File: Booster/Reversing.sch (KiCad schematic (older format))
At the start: 20 parts, among them J701 Conn_01x04, P701 REVERSER_OUT, P702 REVERSER_OUT_OP, Q701 BC817-40, SW701 SW_SPST_x03, U203 LM339, U701 74HC86, U702 PC817

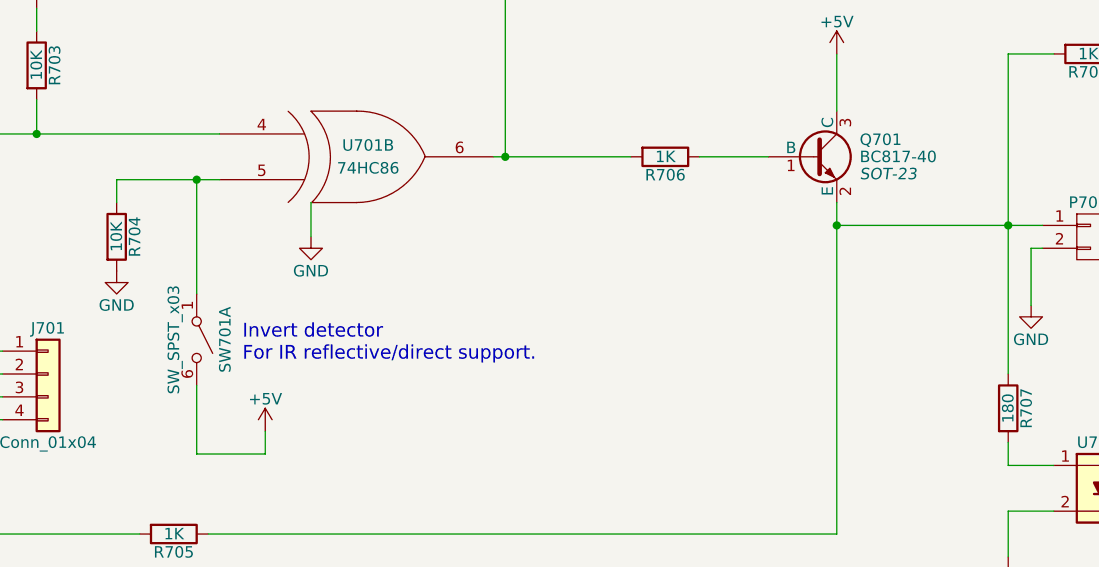
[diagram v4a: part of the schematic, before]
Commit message: Assigned footprints & minor adjustments.
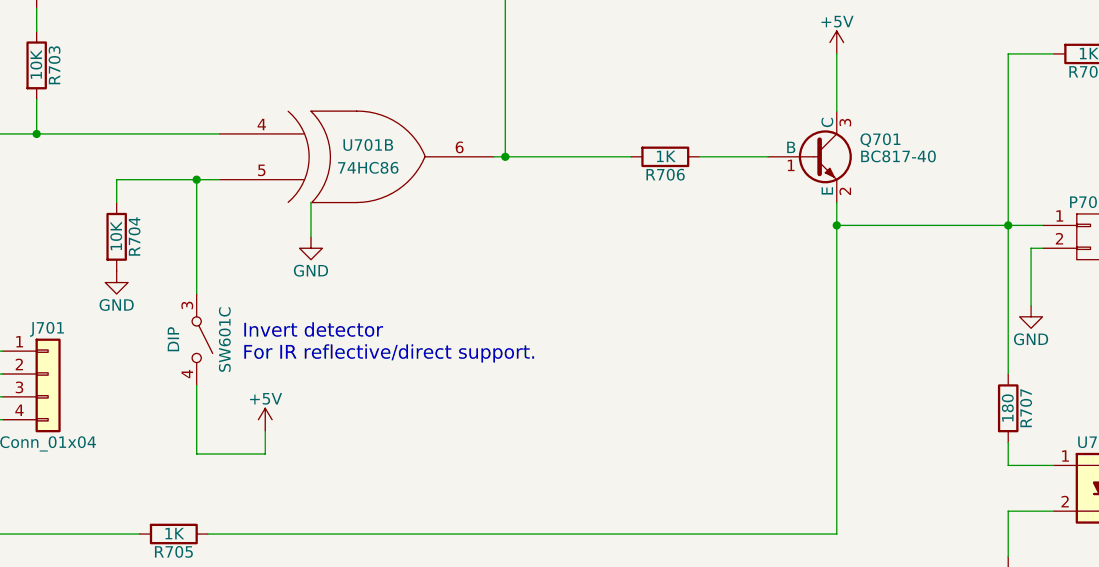
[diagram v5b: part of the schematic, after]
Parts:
- D701: footprint (none) -> LEDs:LED_D3.0mm
- J701: footprint (none) -> Connectors_JST:JST_XH_B04B-XH-A_04x2.50mm_Straight
- P701, P702: footprint (none) -> Connectors_JST:JST_XH_B02B-XH-A_02x2.50mm_Straight
- Q701: footprint SOT-23 -> TO_SOT_Packages_SMD:SOT-23
- R701, R702, R703, R704, R705, R706, R707, R708: footprint (none) -> Resistors_SMD:R_0805
- RV701: footprint (none) -> Potentiometers:Potentiometer_Trimmer_Bourns_3296W
- SW601: renamed from SW701; value SW_SPST_x03 -> DIP; footprint (none) -> Buttons_Switches_THT:SW_DIP_x3_W7.62mm_Slide
- TP701, TP702: footprint (none) -> Measurement_Points:Measurement_Point_Round-TH_Small
- U203, U701: footprint (none) -> SMD_Packages:SOIC-14_N
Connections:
- net +5V: now also SW601.4 (B); no longer SW601.6 (B)
- net at R704.1, U701.5 (IN2): now also SW601.3 (A); no longer SW601.1 (A)
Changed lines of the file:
@@
 F 0 "U701" H 8250 2300 50  0000 C CNN
 F 1 "74HC86" H 8250 2200 50  0000 C CNN
-F 2 "" H 8200 2250 50  0000 C CNN
+F 2 "SMD_Packages:SOIC-14_N" H 8200 2250 50  0001 C CNN
 F 3 "" H 8200 2250 50  0000 C CNN
 	4    8200 2250
@@
 F 0 "R701" V 2330 4300 50  0000 C CNN
 F 1 "10K" V 2250 4300 50  0000 C CNN
-F 2 "" V 2180 4300 50  0000 C CNN
+F 2 "Resistors_SMD:R_0805" V 2180 4300 50  0001 C CNN
 F 3 "" H 2250 4300 50  0000 C CNN
 	1    2250 4300
@@
 F 0 "U203" H 3500 3550 50  0000 L CNN
 F 1 "LM339" H 3500 3150 50  0000 L CNN
-F 2 "" H 3450 3450 50  0000 C CNN
+F 2 "SMD_Packages:SOIC-14_N" H 3450 3450 50  0001 C CNN
 F 3 "" H 3550 3550 50  0000 C CNN
 	1    3500 3350
@@
 F 0 "R703" V 4130 3050 50  0000 C CNN
 F 1 "10K" V 4050 3050 50  0000 C CNN
-F 2 "" V 3980 3050 50  0000 C CNN
+F 2 "Resistors_SMD:R_0805" V 3980 3050 50  0001 C CNN
 F 3 "" H 4050 3050 50  0000 C CNN
 	1    4050 3050
@@
 $EndComp
 $Comp
-L +5V #PWR054
+L +5V #PWR055
 U 1 1 5A08A3B3
 P 4050 2800
-F 0 "#PWR054" H 4050 2650 50  0001 C CNN
+F 0 "#PWR055" H 4050 2650 50  0001 C CNN
 F 1 "+5V" H 4050 2940 50  0000 C CNN
 F 2 "" H 4050 2800 50  0000 C CNN
@@
 F 0 "RV701" V 2375 3250 50  0000 C CNN
 F 1 "POT_TRIM" V 2450 3250 50  0000 C CNN
-F 2 "" H 2550 3250 50  0000 C CNN
+F 2 "Potentiometers:Potentiometer_Trimmer_Bourns_3296W" H 2550 3250 50  0001 C CNN
 F 3 "" H 2550 3250 50  0000 C CNN
 	1    2550 3250
@@
 F 0 "R706" V 6880 3450 50  0000 C CNN
 F 1 "1K" V 6800 3450 50  0000 C CNN
-F 2 "" V 6730 3450 50  0000 C CNN
+F 2 "Resistors_SMD:R_0805" V 6730 3450 50  0001 C CNN
 F 3 "" H 6800 3450 50  0000 C CNN
 	1    6800 3450
@@
 F 0 "D701" H 9100 3100 50  0000 C CNN
 F 1 "LED" H 9100 2900 50  0000 C CNN
-F 2 "" H 9100 3000 50  0000 C CNN
+F 2 "LEDs:LED_D3.0mm" H 9100 3000 50  0001 C CNN
 F 3 "" H 9100 3000 50  0000 C CNN
 	1    9100 3000
@@
 F 0 "R708" V 8730 3000 50  0000 C CNN
 F 1 "1K" V 8650 3000 50  0000 C CNN
-F 2 "" V 8580 3000 50  0000 C CNN
+F 2 "Resistors_SMD:R_0805" V 8580 3000 50  0001 C CNN
 F 3 "" H 8650 3000 50  0000 C CNN
 	1    8650 3000
@@
 $EndComp
 $Comp
-L +5V #PWR055
+L +5V #PWR056
 U 1 1 5A08AC26
 P 7550 3000
-F 0 "#PWR055" H 7550 2850 50  0001 C CNN
+F 0 "#PWR056" H 7550 2850 50  0001 C CNN
 F 1 "+5V" H 7550 3140 50  0000 C CNN
 F 2 "" H 7550 3000 50  0000 C CNN
@@
 $EndComp
 $Comp
-L GND #PWR056
+L GND #PWR057
 U 1 1 5A08AC50
 P 9350 3800
-F 0 "#PWR056" H 9350 3550 50  0001 C CNN
+F 0 "#PWR057" H 9350 3550 50  0001 C CNN
 F 1 "GND" H 9350 3650 50  0000 C CNN
 F 2 "" H 9350 3800 50  0000 C CNN
@@
 F 0 "P701" H 8650 3950 50  0000 C CNN
 F 1 "REVERSER_OUT" V 8750 3800 50  0000 C CNN
-F 2 "" H 8650 3800 50  0000 C CNN
+F 2 "Connectors_JST:JST_XH_B02B-XH-A_02x2.50mm_Straight" H 8650 3800 50  0001 C CNN
 F 3 "" H 8650 3800 50  0000 C CNN
 	1    8650 3800
@@
 $EndComp
 $Comp
-L GND #PWR057
+L GND #PWR058
 U 1 1 5A0EF583
 P 8400 4100
-F 0 "#PWR057" H 8400 3850 50  0001 C CNN
+F 0 "#PWR058" H 8400 3850 50  0001 C CNN
 F 1 "GND" H 8400 3950 50  0000 C CNN
 F 2 "" H 8400 4100 50  0001 C CNN
@@
 F 0 "R707" V 8380 4550 50  0000 C CNN
 F 1 "180" V 8300 4550 50  0000 C CNN
-F 2 "" V 8230 4550 50  0001 C CNN
+F 2 "Resistors_SMD:R_0805" V 8230 4550 50  0001 C CNN
 F 3 "" H 8300 4550 50  0001 C CNN
 	1    8300 4550
@@
 F 0 "P702" H 9600 5050 50  0000 C CNN
 F 1 "REVERSER_OUT_OP" V 9700 4900 50  0000 C CNN
-F 2 "" H 9600 4900 50  0000 C CNN
+F 2 "Connectors_JST:JST_XH_B02B-XH-A_02x2.50mm_Straight" H 9600 4900 50  0001 C CNN
 F 3 "" H 9600 4900 50  0000 C CNN
 	1    9600 4900
@@
 $EndComp
 $Comp
-L GND #PWR058
+L GND #PWR059
 U 1 1 5A0EF7FA
 P 8300 5200
-F 0 "#PWR058" H 8300 4950 50  0001 C CNN
+F 0 "#PWR059" H 8300 4950 50  0001 C CNN
 F 1 "GND" H 8300 5050 50  0000 C CNN
 F 2 "" H 8300 5200 50  0001 C CNN
@@
 F 0 "U701" H 5500 3500 50  0000 C CNN
 F 1 "74HC86" H 5500 3400 50  0000 C CNN
-F 2 "" H 5450 3450 50  0000 C CNN
+F 2 "SMD_Packages:SOIC-14_N" H 5450 3450 50  0001 C CNN
 F 3 "" H 5450 3450 50  0000 C CNN
 	2    5450 3450
@@
 F 0 "R704" V 4480 3800 50  0000 C CNN
 F 1 "10K" V 4400 3800 50  0000 C CNN
-F 2 "" V 4330 3800 50  0000 C CNN
+F 2 "Resistors_SMD:R_0805" V 4330 3800 50  0001 C CNN
 F 3 "" H 4400 3800 50  0000 C CNN
 	1    4400 3800
@@
 $EndComp
 $Comp
-L GND #PWR059
+L GND #PWR060
 U 1 1 5A0F5794
 P 4400 3950
-F 0 "#PWR059" H 4400 3700 50  0001 C CNN
+F 0 "#PWR060" H 4400 3700 50  0001 C CNN
 F 1 "GND" H 4400 3800 50  0000 C CNN
 F 2 "" H 4400 3950 50  0000 C CNN
@@
 $EndComp
 $Comp
-L +5V #PWR060
+L +5V #PWR061
 U 1 1 5A0F5A28
 P 5050 4650
-F 0 "#PWR060" H 5050 4500 50  0001 C CNN
+F 0 "#PWR061" H 5050 4500 50  0001 C CNN
 F 1 "+5V" H 5050 4790 50  0000 C CNN
 F 2 "" H 5050 4650 50  0001 C CNN
@@
 F 0 "R702" V 2330 4500 50  0000 C CNN
 F 1 "220" V 2250 4500 50  0000 C CNN
-F 2 "" V 2180 4500 50  0000 C CNN
+F 2 "Resistors_SMD:R_0805" V 2180 4500 50  0001 C CNN
 F 3 "" H 2250 4500 50  0000 C CNN
 	1    2250 4500
@@
 IR_Led
 $Comp
-L +5V #PWR061
+L +5V #PWR062
 U 1 1 5A0FEE2F
 P 8000 1800
-F 0 "#PWR061" H 8000 1650 50  0001 C CNN
+F 0 "#PWR062" H 8000 1650 50  0001 C CNN
 F 1 "+5V" H 8000 1940 50  0000 C CNN
 F 2 "" H 8000 1800 50  0001 C CNN
@@
 F 0 "R705" V 4730 5100 50  0000 C CNN
 F 1 "1K" V 4650 5100 50  0000 C CNN
-F 2 "" V 4580 5100 50  0001 C CNN
+F 2 "Resistors_SMD:R_0805" V 4580 5100 50  0001 C CNN
 F 3 "" H 4650 5100 50  0001 C CNN
 	1    4650 5100
@@
 F 0 "J701" H 4100 4600 50  0000 C CNN
 F 1 "Conn_01x04" H 4100 4100 50  0000 C CNN
-F 2 "" H 4100 4400 50  0001 C CNN
+F 2 "Connectors_JST:JST_XH_B04B-XH-A_04x2.50mm_Straight" H 4100 4400 50  0001 C CNN
 F 3 "" H 4100 4400 50  0001 C CNN
 	1    4100 4400
@@
 	3800 4600 3800 4700
 $Comp
-L GND #PWR062
+L GND #PWR063
 U 1 1 5A101A8A
 P 3800 4700
-F 0 "#PWR062" H 3800 4450 50  0001 C CNN
+F 0 "#PWR063" H 3800 4450 50  0001 C CNN
 F 1 "GND" H 3800 4550 50  0000 C CNN
 F 2 "" H 3800 4700 50  0001 C CNN
@@
 $EndComp
 $Comp
-L +5V #PWR063
+L +5V #PWR064
 U 1 1 5A104760
 P 1950 4150
-F 0 "#PWR063" H 1950 4000 50  0001 C CNN
+F 0 "#PWR064" H 1950 4000 50  0001 C CNN
 F 1 "+5V" H 1950 4290 50  0000 C CNN
 F 2 "" H 1950 4150 50  0001 C CNN
@@
 	1950 4150 1950 4500
 $Comp
-L SW_SPST_x03 SW701
-U 1 1 5A1068DB
+L SW_SPST_x03 SW601
+U 3 1 5A1068DB
 P 4750 4250
-F 0 "SW701" H 4750 4375 50  0000 C CNN
-F 1 "SW_SPST_x03" H 4750 4150 50  0000 C CNN
-F 2 "" H 4750 4250 50  0001 C CNN
+F 0 "SW601" H 4750 4375 50  0000 C CNN
+F 1 "DIP" H 4750 4150 50  0000 C CNN
+F 2 "Buttons_Switches_THT:SW_DIP_x3_W7.62mm_Slide" H 4750 4250 50  0001 C CNN
 F 3 "" H 4750 4250 50  0001 C CNN
-	1    4750 4250
+	3    4750 4250
 	0    1    1    0
 $EndComp
@@
 F 0 "TP701" H 3050 3550 50  0000 C BNN
 F 1 "TEST" H 3050 3500 50  0000 C CNN
-F 2 "" H 3050 3250 50  0001 C CNN
+F 2 "Measurement_Points:Measurement_Point_Round-TH_Small" H 3050 3250 50  0001 C CNN
 F 3 "" H 3050 3250 50  0001 C CNN
 	1    3050 3250
@@
 F 0 "TP702" H 3050 3750 50  0000 C BNN
 F 1 "TEST" H 3050 3700 50  0000 C CNN
-F 2 "" H 3050 3450 50  0001 C CNN
+F 2 "Measurement_Points:Measurement_Point_Round-TH_Small" H 3050 3450 50  0001 C CNN
 F 3 "" H 3050 3450 50  0001 C CNN
 	1    3050 3450
@@
 	2200 2800 2200 3000
 $Comp
-L GND #PWR064
+L GND #PWR065
 U 1 1 5A19FF1E
 P 2200 3000
-F 0 "#PWR064" H 2200 2750 50  0001 C CNN
+F 0 "#PWR065" H 2200 2750 50  0001 C CNN
 F 1 "GND" H 2200 2850 50  0000 C CNN
 F 2 "" H 2200 3000 50  0000 C CNN
@@
 $EndComp
 $Comp
-L GND #PWR065
+L GND #PWR066
 U 1 1 5A397E1F
 P 5250 3800
-F 0 "#PWR065" H 5250 3550 50  0001 C CNN
+F 0 "#PWR066" H 5250 3550 50  0001 C CNN
 F 1 "GND" H 5250 3650 50  0000 C CNN
 F 2 "" H 5250 3800 50  0001 C CNN
@@
 F 0 "Q701" H 7650 3525 50  0000 L CNN
 F 1 "BC817-40" H 7650 3450 50  0000 L CNN
-F 2 "SOT-23" H 7650 3375 50  0000 L CIN
+F 2 "TO_SOT_Packages_SMD:SOT-23" H 7650 3375 50  0001 L CIN
 F 3 "" H 7450 3450 50  0000 L CNN
 	1    7450 3450

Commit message: Starting to add traces. Minor schematic changes to aid routing.
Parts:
- U702: footprint Housings_DIP:DIP-4_W7.62mm -> Housings_DIP:SMDIP-4_W9.53mm_Clearance8mm
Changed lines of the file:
@@
 $EndComp
 $Comp
-L +5V #PWR055
+L +5V #PWR704
 U 1 1 5A08A3B3
 P 4050 2800
-F 0 "#PWR055" H 4050 2650 50  0001 C CNN
+F 0 "#PWR704" H 4050 2650 50  0001 C CNN
 F 1 "+5V" H 4050 2940 50  0000 C CNN
 F 2 "" H 4050 2800 50  0000 C CNN
@@
 $EndComp
 $Comp
-L +5V #PWR056
+L +5V #PWR708
 U 1 1 5A08AC26
 P 7550 3000
-F 0 "#PWR056" H 7550 2850 50  0001 C CNN
+F 0 "#PWR708" H 7550 2850 50  0001 C CNN
 F 1 "+5V" H 7550 3140 50  0000 C CNN
 F 2 "" H 7550 3000 50  0000 C CNN
@@
 $EndComp
 $Comp
-L GND #PWR057
+L GND #PWR712
 U 1 1 5A08AC50
 P 9350 3800
-F 0 "#PWR057" H 9350 3550 50  0001 C CNN
+F 0 "#PWR712" H 9350 3550 50  0001 C CNN
 F 1 "GND" H 9350 3650 50  0000 C CNN
 F 2 "" H 9350 3800 50  0000 C CNN
@@
 $EndComp
 $Comp
-L GND #PWR058
+L GND #PWR711
 U 1 1 5A0EF583
 P 8400 4100
-F 0 "#PWR058" H 8400 3850 50  0001 C CNN
+F 0 "#PWR711" H 8400 3850 50  0001 C CNN
 F 1 "GND" H 8400 3950 50  0000 C CNN
 F 2 "" H 8400 4100 50  0001 C CNN
@@
 F 0 "U702" H 8600 5100 50  0000 L CNN
 F 1 "PC817" H 8800 5100 50  0000 L CNN
-F 2 "Housings_DIP:DIP-4_W7.62mm" H 8600 4700 50  0001 L CIN
+F 2 "Housings_DIP:SMDIP-4_W9.53mm_Clearance8mm" H 8600 4700 50  0001 L CIN
 F 3 "" H 8800 4900 50  0001 L CNN
 	1    8800 4900
@@
 $EndComp
 $Comp
-L GND #PWR059
+L GND #PWR710
 U 1 1 5A0EF7FA
 P 8300 5200
-F 0 "#PWR059" H 8300 4950 50  0001 C CNN
+F 0 "#PWR710" H 8300 4950 50  0001 C CNN
 F 1 "GND" H 8300 5050 50  0000 C CNN
 F 2 "" H 8300 5200 50  0001 C CNN
@@
 $EndComp
 $Comp
-L GND #PWR060
+L GND #PWR705
 U 1 1 5A0F5794
 P 4400 3950
-F 0 "#PWR060" H 4400 3700 50  0001 C CNN
+F 0 "#PWR705" H 4400 3700 50  0001 C CNN
 F 1 "GND" H 4400 3800 50  0000 C CNN
 F 2 "" H 4400 3950 50  0000 C CNN
@@
 $EndComp
 $Comp
-L +5V #PWR061
+L +5V #PWR706
 U 1 1 5A0F5A28
 P 5050 4650
-F 0 "#PWR061" H 5050 4500 50  0001 C CNN
+F 0 "#PWR706" H 5050 4500 50  0001 C CNN
 F 1 "+5V" H 5050 4790 50  0000 C CNN
 F 2 "" H 5050 4650 50  0001 C CNN
@@
 IR_Led
 $Comp
-L +5V #PWR062
+L +5V #PWR709
 U 1 1 5A0FEE2F
 P 8000 1800
-F 0 "#PWR062" H 8000 1650 50  0001 C CNN
+F 0 "#PWR709" H 8000 1650 50  0001 C CNN
 F 1 "+5V" H 8000 1940 50  0000 C CNN
 F 2 "" H 8000 1800 50  0001 C CNN
@@
 	3800 4600 3800 4700
 $Comp
-L GND #PWR063
+L GND #PWR703
 U 1 1 5A101A8A
 P 3800 4700
-F 0 "#PWR063" H 3800 4450 50  0001 C CNN
+F 0 "#PWR703" H 3800 4450 50  0001 C CNN
 F 1 "GND" H 3800 4550 50  0000 C CNN
 F 2 "" H 3800 4700 50  0001 C CNN
@@
 $EndComp
 $Comp
-L +5V #PWR064
+L +5V #PWR701
 U 1 1 5A104760
 P 1950 4150
-F 0 "#PWR064" H 1950 4000 50  0001 C CNN
+F 0 "#PWR701" H 1950 4000 50  0001 C CNN
 F 1 "+5V" H 1950 4290 50  0000 C CNN
 F 2 "" H 1950 4150 50  0001 C CNN
@@
 	2200 2800 2200 3000
 $Comp
-L GND #PWR065
+L GND #PWR702
 U 1 1 5A19FF1E
 P 2200 3000
-F 0 "#PWR065" H 2200 2750 50  0001 C CNN
+F 0 "#PWR702" H 2200 2750 50  0001 C CNN
 F 1 "GND" H 2200 2850 50  0000 C CNN
 F 2 "" H 2200 3000 50  0000 C CNN
@@
 $EndComp
 $Comp
-L GND #PWR066
+L GND #PWR707
 U 1 1 5A397E1F
 P 5250 3800
-F 0 "#PWR066" H 5250 3550 50  0001 C CNN
+F 0 "#PWR707" H 5250 3550 50  0001 C CNN
 F 1 "GND" H 5250 3650 50  0000 C CNN
 F 2 "" H 5250 3800 50  0001 C CNN

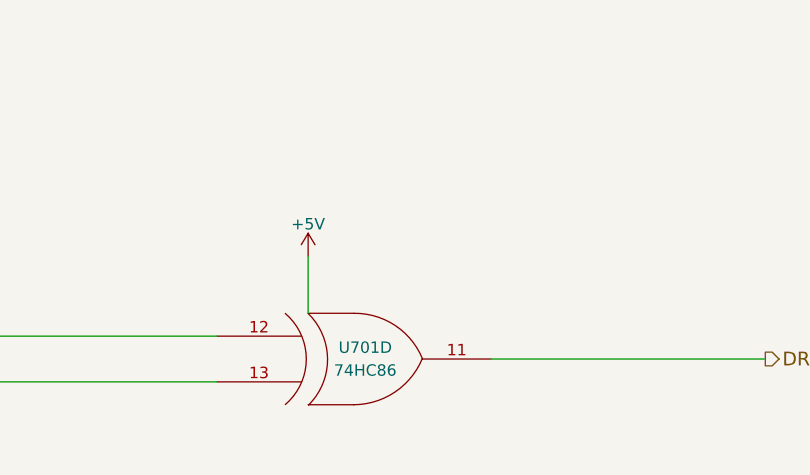
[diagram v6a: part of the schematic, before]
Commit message: First full layout pass of the PCB.
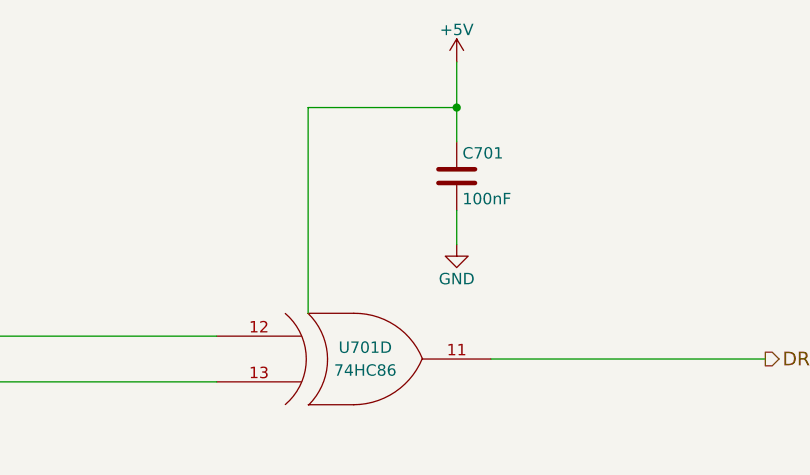
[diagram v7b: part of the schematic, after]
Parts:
- added C701: 100nF, Capacitors_SMD:C_0805, symbol C
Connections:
- net +5V: now also C701.1
- net GND: now also C701.2
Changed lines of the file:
@@
 $EndComp
 $Comp
-L +5V #PWR704
+L +5V #PWR055
 U 1 1 5A08A3B3
 P 4050 2800
-F 0 "#PWR704" H 4050 2650 50  0001 C CNN
+F 0 "#PWR055" H 4050 2650 50  0001 C CNN
 F 1 "+5V" H 4050 2940 50  0000 C CNN
 F 2 "" H 4050 2800 50  0000 C CNN
@@
 $EndComp
 $Comp
-L +5V #PWR708
+L +5V #PWR056
 U 1 1 5A08AC26
 P 7550 3000
-F 0 "#PWR708" H 7550 2850 50  0001 C CNN
+F 0 "#PWR056" H 7550 2850 50  0001 C CNN
 F 1 "+5V" H 7550 3140 50  0000 C CNN
 F 2 "" H 7550 3000 50  0000 C CNN
@@
 $EndComp
 $Comp
-L GND #PWR712
+L GND #PWR057
 U 1 1 5A08AC50
 P 9350 3800
-F 0 "#PWR712" H 9350 3550 50  0001 C CNN
+F 0 "#PWR057" H 9350 3550 50  0001 C CNN
 F 1 "GND" H 9350 3650 50  0000 C CNN
 F 2 "" H 9350 3800 50  0000 C CNN
@@
 $EndComp
 $Comp
-L GND #PWR711
+L GND #PWR058
 U 1 1 5A0EF583
 P 8400 4100
-F 0 "#PWR711" H 8400 3850 50  0001 C CNN
+F 0 "#PWR058" H 8400 3850 50  0001 C CNN
 F 1 "GND" H 8400 3950 50  0000 C CNN
 F 2 "" H 8400 4100 50  0001 C CNN
@@
 $EndComp
 $Comp
-L GND #PWR710
+L GND #PWR059
 U 1 1 5A0EF7FA
 P 8300 5200
-F 0 "#PWR710" H 8300 4950 50  0001 C CNN
+F 0 "#PWR059" H 8300 4950 50  0001 C CNN
 F 1 "GND" H 8300 5050 50  0000 C CNN
 F 2 "" H 8300 5200 50  0001 C CNN
@@
 $EndComp
 $Comp
-L GND #PWR705
+L GND #PWR060
 U 1 1 5A0F5794
 P 4400 3950
-F 0 "#PWR705" H 4400 3700 50  0001 C CNN
+F 0 "#PWR060" H 4400 3700 50  0001 C CNN
 F 1 "GND" H 4400 3800 50  0000 C CNN
 F 2 "" H 4400 3950 50  0000 C CNN
@@
 $EndComp
 $Comp
-L +5V #PWR706
+L +5V #PWR061
 U 1 1 5A0F5A28
 P 5050 4650
-F 0 "#PWR706" H 5050 4500 50  0001 C CNN
+F 0 "#PWR061" H 5050 4500 50  0001 C CNN
 F 1 "+5V" H 5050 4790 50  0000 C CNN
 F 2 "" H 5050 4650 50  0001 C CNN
@@
 IR_Led
 $Comp
-L +5V #PWR709
+L +5V #PWR062
 U 1 1 5A0FEE2F
-P 8000 1800
-F 0 "#PWR709" H 8000 1650 50  0001 C CNN
-F 1 "+5V" H 8000 1940 50  0000 C CNN
-F 2 "" H 8000 1800 50  0001 C CNN
-F 3 "" H 8000 1800 50  0001 C CNN
-	1    8000 1800
+P 8650 950
+F 0 "#PWR062" H 8650 800 50  0001 C CNN
+F 1 "+5V" H 8650 1090 50  0000 C CNN
+F 2 "" H 8650 950 50  0001 C CNN
+F 3 "" H 8650 950 50  0001 C CNN
+	1    8650 950
 	1    0    0    -1
 $EndComp
@@
 	3900 4500 3700 4500
 Wire Wire Line
-	8000 2050 8000 1800
+	8000 1150 8000 2050
 Wire Wire Line
 	5050 4750 4750 4750
@@
 	3800 4600 3800 4700
 $Comp
-L GND #PWR703
+L GND #PWR063
 U 1 1 5A101A8A
 P 3800 4700
-F 0 "#PWR703" H 3800 4450 50  0001 C CNN
+F 0 "#PWR063" H 3800 4450 50  0001 C CNN
 F 1 "GND" H 3800 4550 50  0000 C CNN
 F 2 "" H 3800 4700 50  0001 C CNN
@@
 $EndComp
 $Comp
-L +5V #PWR701
+L +5V #PWR064
 U 1 1 5A104760
 P 1950 4150
-F 0 "#PWR701" H 1950 4000 50  0001 C CNN
+F 0 "#PWR064" H 1950 4000 50  0001 C CNN
 F 1 "+5V" H 1950 4290 50  0000 C CNN
 F 2 "" H 1950 4150 50  0001 C CNN
@@
 	2200 2800 2200 3000
 $Comp
-L GND #PWR702
+L GND #PWR065
 U 1 1 5A19FF1E
 P 2200 3000
-F 0 "#PWR702" H 2200 2750 50  0001 C CNN
+F 0 "#PWR065" H 2200 2750 50  0001 C CNN
 F 1 "GND" H 2200 2850 50  0000 C CNN
 F 2 "" H 2200 3000 50  0000 C CNN
@@
 $EndComp
 $Comp
-L GND #PWR707
+L GND #PWR066
 U 1 1 5A397E1F
 P 5250 3800
-F 0 "#PWR707" H 5250 3550 50  0001 C CNN
+F 0 "#PWR066" H 5250 3550 50  0001 C CNN
 F 1 "GND" H 5250 3650 50  0000 C CNN
 F 2 "" H 5250 3800 50  0001 C CNN
@@
 	8500 3000 8300 3000
 Connection ~ 7550 3750
+$Comp
+L C C701
+U 1 1 5A462A8A
+P 8650 1450
+F 0 "C701" H 8675 1550 50  0000 L CNN
+F 1 "100nF" H 8675 1350 50  0000 L CNN
+F 2 "Capacitors_SMD:C_0805" H 8688 1300 50  0001 C CNN
+F 3 "" H 8650 1450 50  0001 C CNN
+	1    8650 1450
+	1    0    0    -1
+$EndComp
+Wire Wire Line
+	8650 1600 8650 1750
+$Comp
+L GND #PWR067
+U 1 1 5A462BB8
+P 8650 1750
+F 0 "#PWR067" H 8650 1500 50  0001 C CNN
+F 1 "GND" H 8650 1600 50  0000 C CNN
+F 2 "" H 8650 1750 50  0001 C CNN
+F 3 "" H 8650 1750 50  0001 C CNN
+	1    8650 1750
+	1    0    0    -1
+$EndComp
+Wire Wire Line
+	8650 950  8650 1300
+Wire Wire Line
+	8000 1150 8650 1150
+Connection ~ 8650 1150
 $EndSCHEMATC
